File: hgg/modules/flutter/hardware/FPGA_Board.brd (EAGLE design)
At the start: 100 x 77 mm, 89 parts, among them IC1 AT45DB161D-SU, IC2 MEGA8-AI, IC3 MAX481CSA, Q1 8Mhz, U2 XC3S50AVQ100, X1 BU-SMA-V, X2 MINI-USB-32005-201

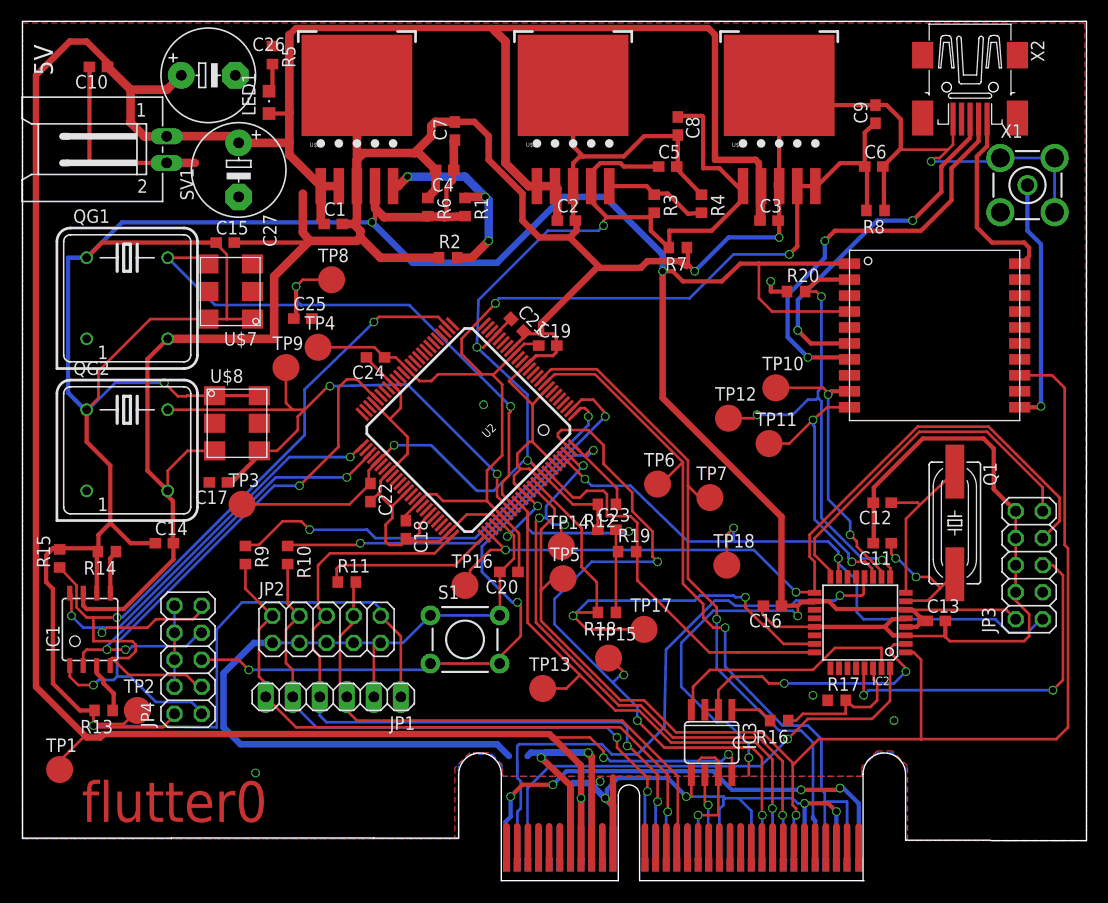
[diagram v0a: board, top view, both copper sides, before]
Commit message: - 0mil thermal isolation space between cooling pads and ground plane - deleted one misrouted signal path - added info text to layout
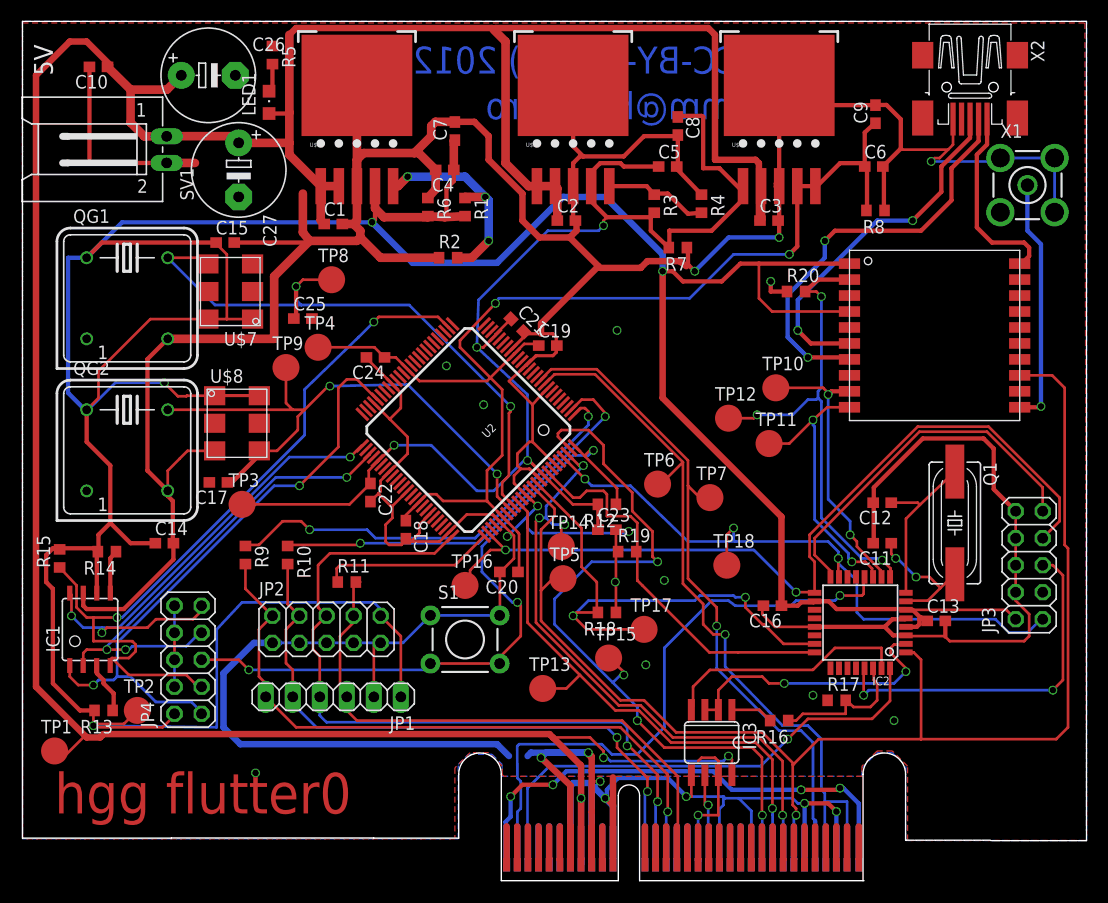
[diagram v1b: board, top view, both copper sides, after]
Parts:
- moved TP1 1.81 mm to (3.02, 11.4)
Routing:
- net VCC3.3: track 402.7 -> 373.8 mm, vias 6 -> 4
- net VCC1.2: track 115.5 -> 116.0 mm
- net GND: vias 18 -> 23
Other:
- board text added: "(CC-BY-NC-SA) 2012"
- board text added: "hgg flutter0"
- board text added: "timm@hgg.aero"
- board text removed: "flutter0"
